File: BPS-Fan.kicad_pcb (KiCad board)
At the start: 2 copper layers, 57.9 x 68.1 mm, 37 parts, among them J1 LDRBRDConn, J10 FAN9, J11 FAN10, J12 FAN11, J13 FAN12, J2 FAN1, J3 FAN2, J4 FAN3, J5 FAN4, J6 FAN5, J7 FAN6, J8 FAN7, J9 FAN8, Q1 BUK9M23-80E, Q2 BUK9M23-80E, Q3 BUK9M23-80E, Q4 BUK9M23-80E

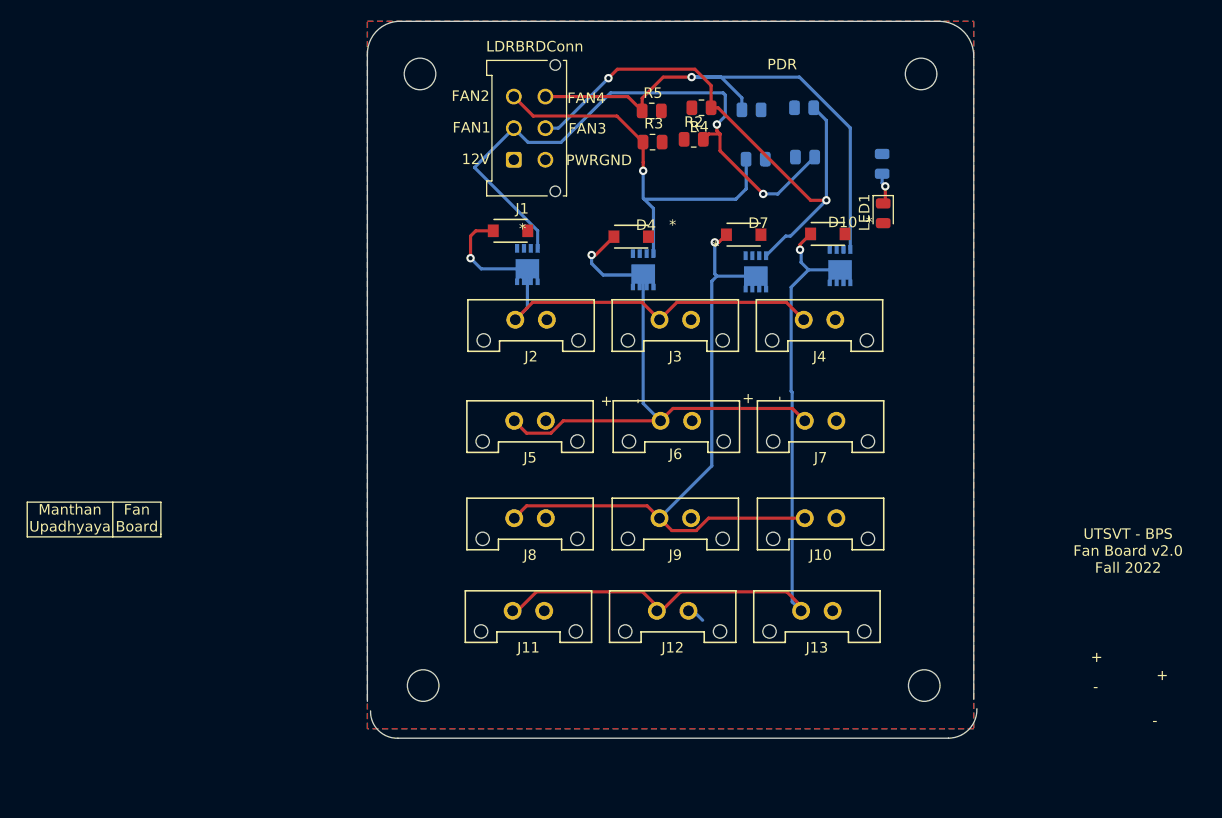
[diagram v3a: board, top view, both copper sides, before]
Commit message: Complete layout of fan board
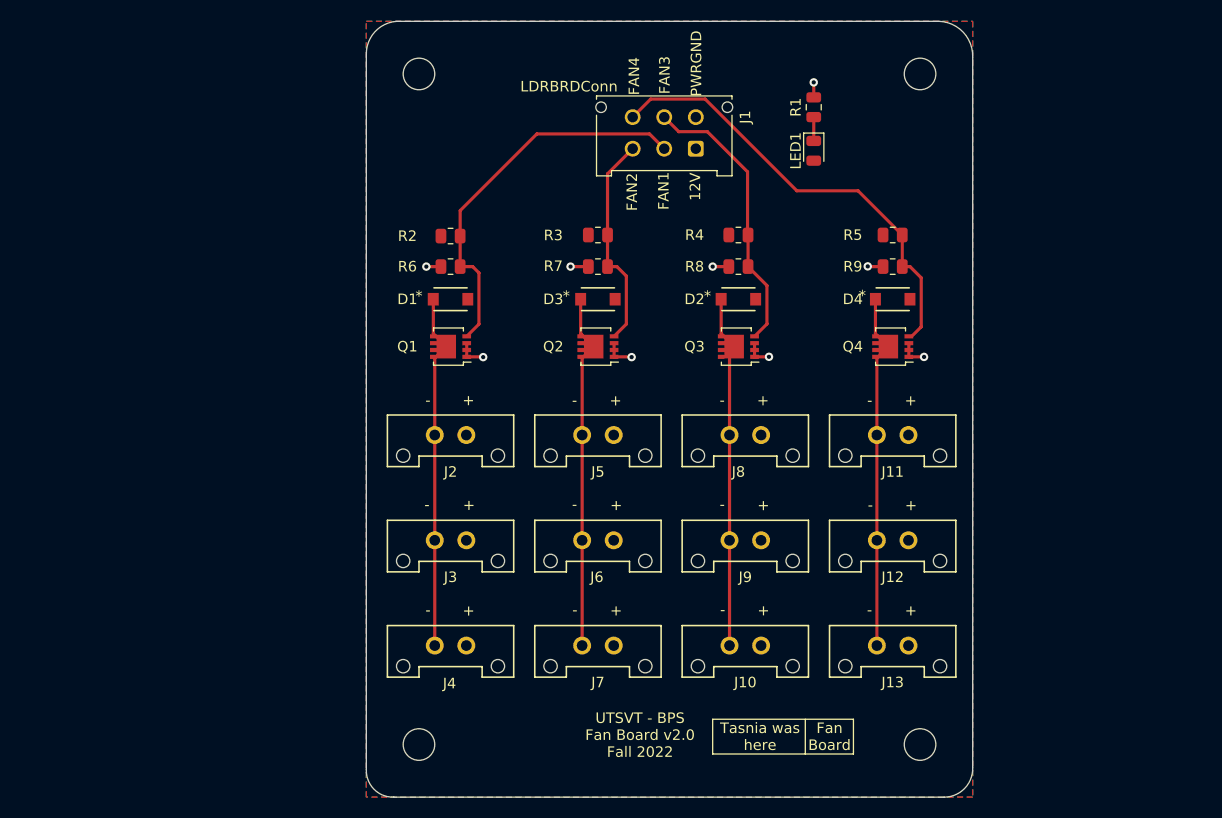
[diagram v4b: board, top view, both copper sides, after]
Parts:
- Q1, Q2, Q3, Q4, R1, R6, R7, R8, R9: moved to F.Cu
- moved J4 46.8 mm to (138.0, 100.0)
- moved J11 38.4 mm to (180.0, 80.0)
- moved R6 35.2 mm to (136.5, 64.0)
- moved J7 30.1 mm to (152.0, 100.0)
- moved J3 29.9 mm to (138.0, 90.0)
- moved LOGO1 28.9 mm to (143.3, 63.0)
- moved R5 25.7 mm to (178.5, 61.0), turned to 0 degrees
- moved R2 24.9 mm to (136.5, 61.1)
- moved J12 21.9 mm to (180.0, 90.0)
- moved J8 21.9 mm to (166.0, 80.0)
- moved R9 20.0 mm to (178.5, 64.0), turned to 180 degrees
- moved LOGO2 18.7 mm to (159.1, 63.4)
- moved R7 18.1 mm to (150.5, 64.0), turned to 180 degrees
- moved J1 17.3 mm to (159.8, 52.8), turned to 180 degrees
- moved R8 16.3 mm to (163.8, 64.0)
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- renumbered D7 to D2, D4 to D3, D10 to D4
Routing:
- net Net-(D4-Pad2): track 71.0 -> 33.9 mm, vias 1 -> 0
- net Net-(D2-Pad2): track 63.6 -> 33.6 mm, vias 1 -> 0
- net /FAN3_BPS: track 52.7 -> 26.9 mm, vias 2 -> 0
- net /FAN1_BPS: track 58.2 -> 36.8 mm, vias 2 -> 0
- net Net-(D3-Pad2): track 53.5 -> 33.9 mm, vias 1 -> 0
- net GNDPWR: track 0.42 -> 18.7 mm, vias 0 -> 9
- net /FAN2_BPS: track 38.2 -> 20.6 mm, vias 1 -> 0
- net Net-(D1-Pad2): track 46.1 -> 33.9 mm, vias 1 -> 0
- net /FAN4_BPS: track 51.8 -> 42.8 mm, vias 1 -> 0
- net +12V: track 4.46 -> 0.00 mm
- net Net-(LED1-Pad1): track 3.03 -> 2.16 mm, vias 1 -> 0
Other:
- board size 57.9 x 68.1 mm -> 57.6 x 73.7 mm
- board text added: "Tasnia was here"
- board text removed: "Manthan Upadhyaya"
- board text removed: "PDR"

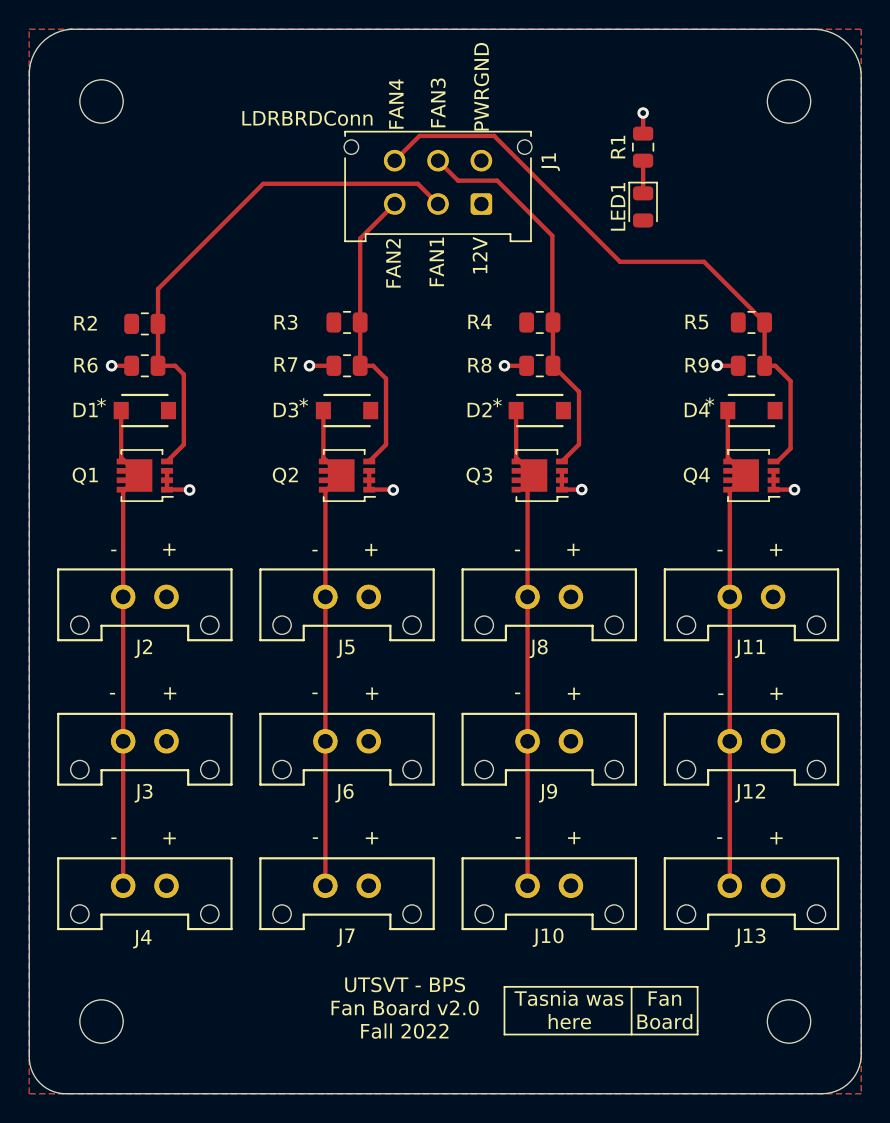
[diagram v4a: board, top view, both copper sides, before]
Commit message: fixed user user comments for dimensions
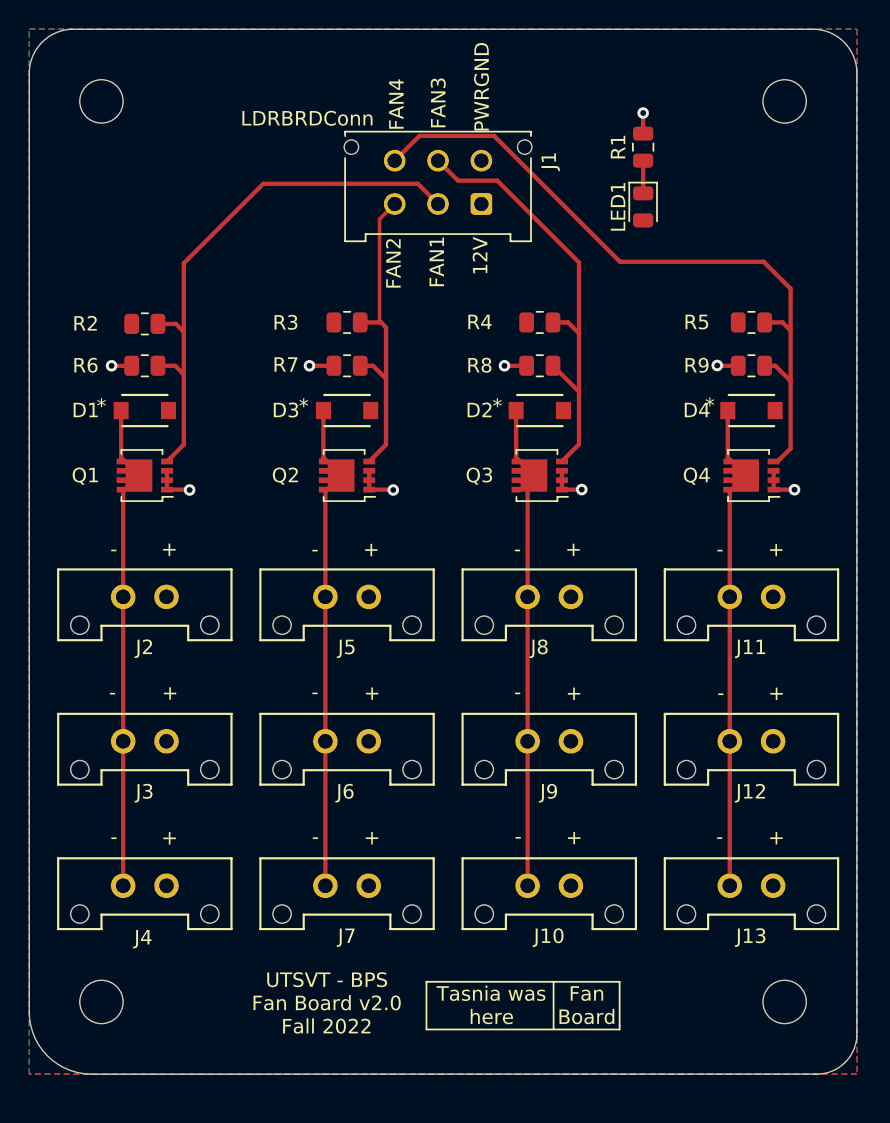
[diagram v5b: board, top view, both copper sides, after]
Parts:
- moved H2 1.39 mm to (180.8, 108.0)
- moved H4 1.35 mm to (133.5, 108.0)
- moved H3 0.30 mm to (180.8, 45.7)
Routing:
- net /FAN4_BPS: track 42.8 -> 49.1 mm
- net /FAN3_BPS: track 26.9 -> 31.6 mm
- net /FAN1_BPS: track 36.8 -> 38.7 mm
- net /FAN2_BPS: track 20.6 -> 22.4 mm
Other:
- board size 57.6 x 73.7 mm -> 57.3 x 72.3 mm

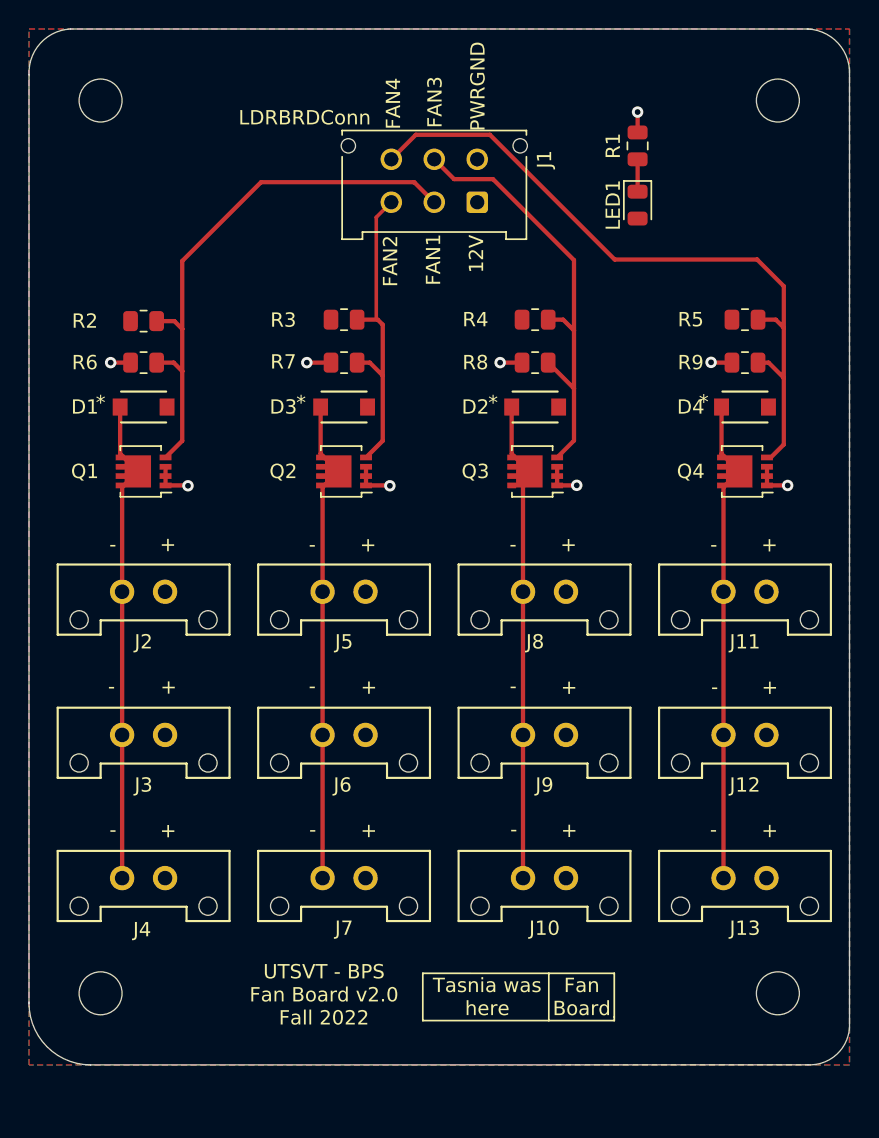
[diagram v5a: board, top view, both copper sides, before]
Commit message: added space between connectors as suggested by Raymond
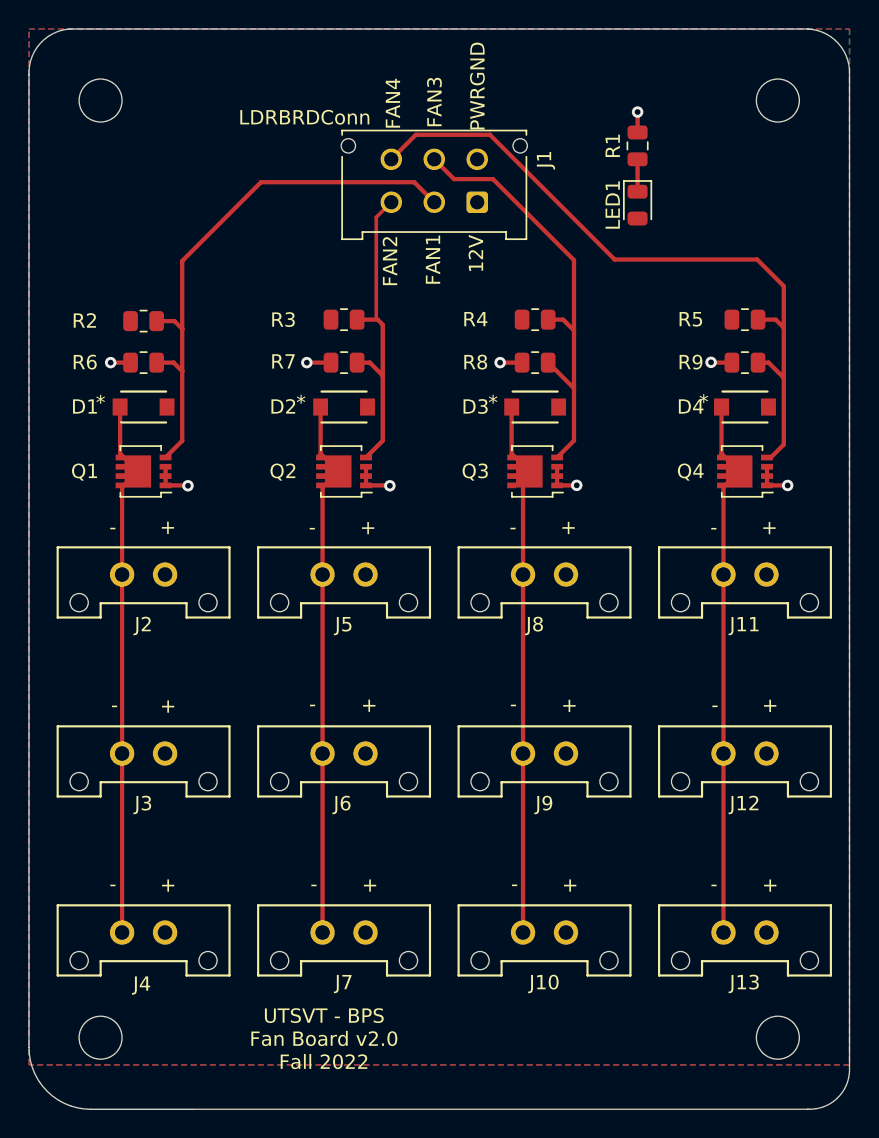
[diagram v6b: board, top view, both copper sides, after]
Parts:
- moved J10 3.80 mm to (166.0, 103.8)
- moved J13 3.80 mm to (180.0, 103.8)
- moved J4 3.80 mm to (138.0, 103.8)
- moved J7 3.80 mm to (152.0, 103.8)
- moved H2 3.10 mm to (180.8, 111.1)
- moved H4 3.10 mm to (133.5, 111.1)
- moved J12 1.30 mm to (180.0, 91.3)
- moved J3 1.30 mm to (138.0, 91.3)
- moved J6 1.30 mm to (152.0, 91.3)
- moved J9 1.30 mm to (166.0, 91.3)
- moved J11 1.20 mm to (180.0, 78.8)
- moved J2 1.20 mm to (138.0, 78.8)
- moved J5 1.20 mm to (152.0, 78.8)
- moved J8 1.20 mm to (166.0, 78.8)
- renumbered D3 to D2, D2 to D3
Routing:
- net Net-(D1-Pad2): track 33.9 -> 37.9 mm
- net Net-(D4-Pad2): track 33.9 -> 37.7 mm
- net Net-(D3-Pad2): track 33.6 -> 37.4 mm
- net Net-(D2-Pad2): track 33.9 -> 37.7 mm
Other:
- board size 57.3 x 72.3 mm -> 57.3 x 75.4 mm
- board text removed: "Fan Board"
- board text removed: "Tasnia was here"

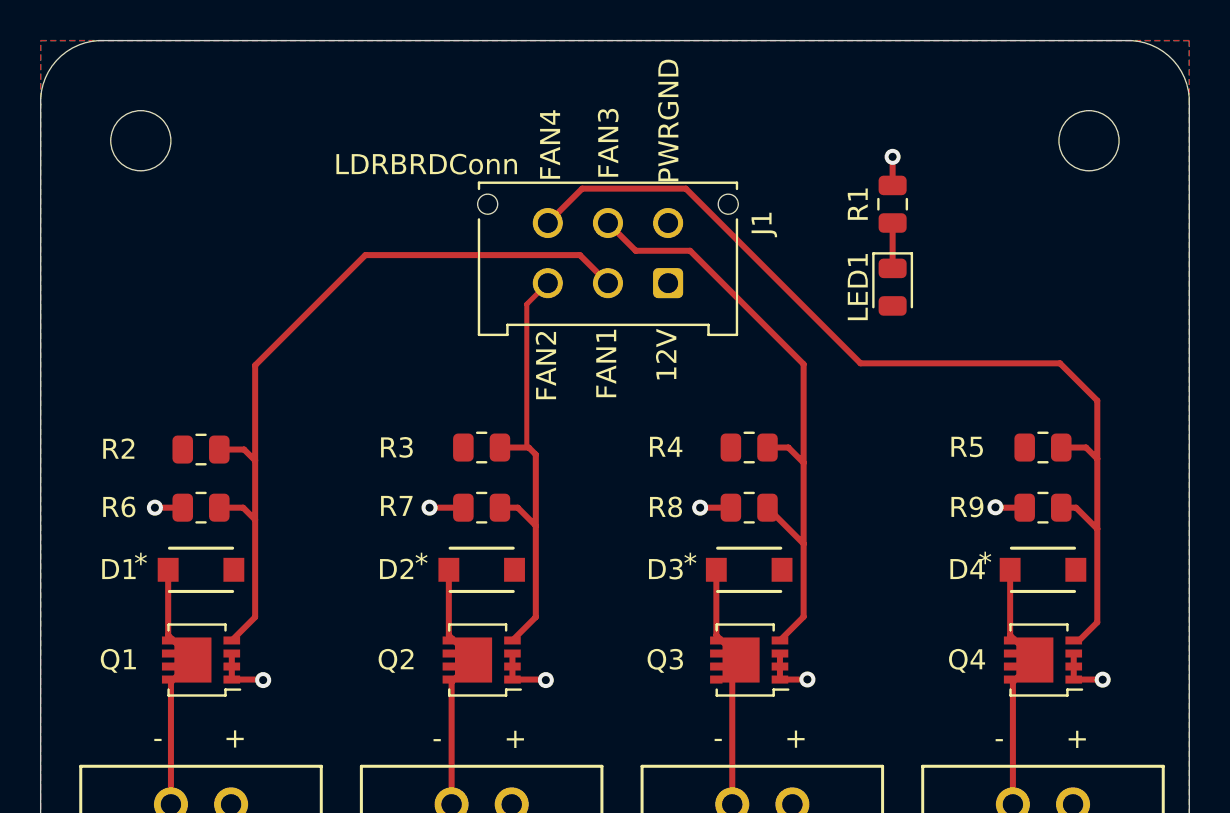
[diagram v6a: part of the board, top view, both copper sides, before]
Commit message: made GNDPWR traces and vias bigger, made drill files and gerber files
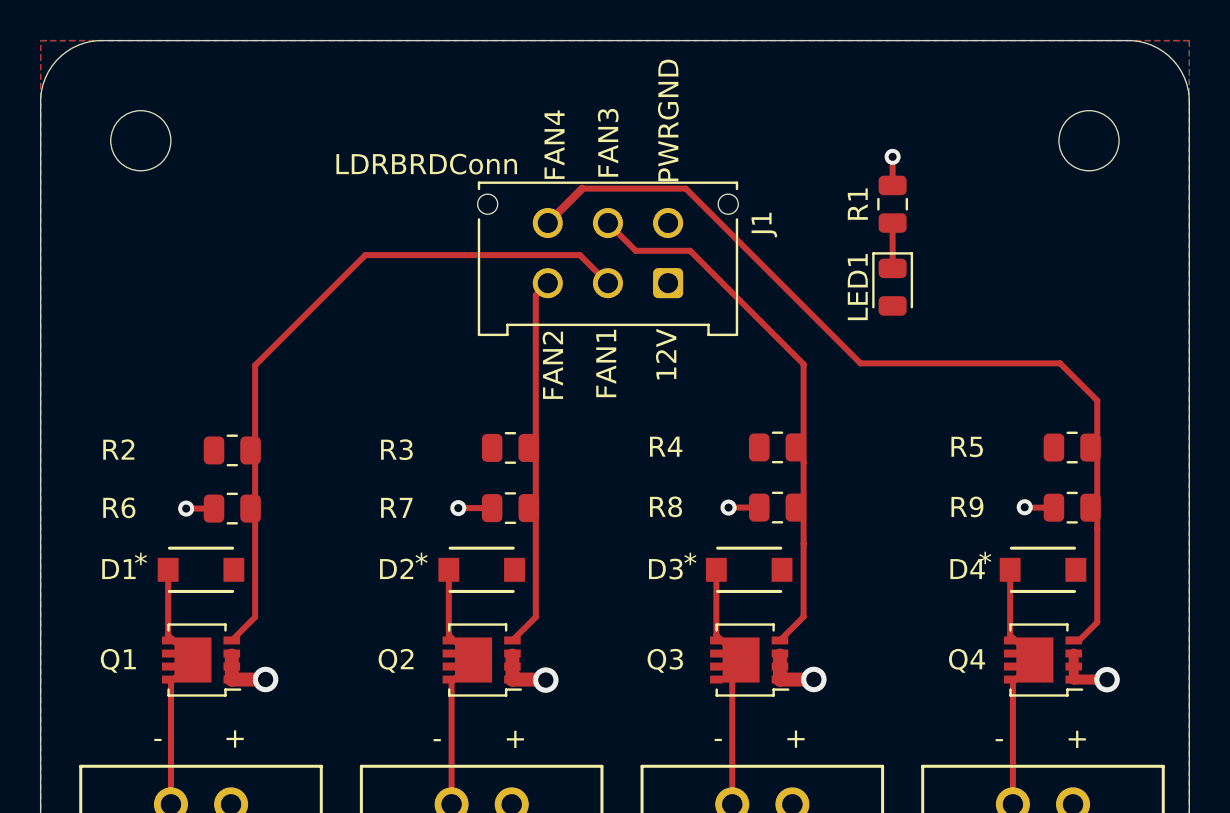
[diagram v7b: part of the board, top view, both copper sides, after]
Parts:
- moved R2 1.56 mm to (138.1, 61.1)
- moved R6 1.56 mm to (138.1, 64.0)
- moved R5 1.46 mm to (180.0, 61.0)
- moved R9 1.46 mm to (180.0, 64.0)
- moved R7 1.43 mm to (151.9, 64.0)
- moved R3 1.43 mm to (151.9, 61.0)
- moved LOGO2 1.43 mm to (158.2, 62.3)
- moved R4 1.41 mm to (165.3, 61.0)
- moved R8 1.41 mm to (165.3, 64.0)
- moved LOGO1 1.40 mm to (141.9, 63.3)
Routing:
- net /FAN3_BPS: track 31.6 -> 26.9 mm
- net /FAN4_BPS: track 49.1 -> 44.8 mm
- net /FAN1_BPS: track 38.7 -> 34.7 mm
- net /FAN2_BPS: track 22.4 -> 18.6 mm
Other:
- rule pad_to_mask_clearance: 0.05 -> 0
